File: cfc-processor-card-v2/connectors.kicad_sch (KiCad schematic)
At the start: 9 parts, among them J1 ORESAT-DEBUG-CONNECTOR-ALL, J2 J-SAMTEC-TFM-110-X1-XXX-D-RA, J4 TFM-120-01-L-D-RA, U1 RCLAMP0504FB

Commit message: Clean up CFC Processor Card from Scott's initial import which was Gerber identical to origianl EAGLE schematic. Interestingly, this version was already changed for the v2 backplane which is great. Align schematic to be more KiCAD like based off of the C3, rename a few things, remove some outdated OPD connections, import sch into pcb, clean up pcb detritus, and import DRU settings. No longer Gerber identicial, but it's now ready for further polishing for fabrication.
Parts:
- removed TP183, TP184: TEST-POINT3X4, cfc-card:PAD.03X.04, symbol cfc-card-eagle-import:TEST-POINT3X4
- removed U$1: FLIGHMARKERNEW, cfc-card:FLIGHTMARKER_NEW_BOARDS, symbol cfc-card-eagle-import:FLIGHMARKERNEW
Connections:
- net GND: no longer J4.37, J4.38
- net CAN1_H: no longer names the net of J4.33, J4.34
- net CAN1_L: no longer names the net of J4.35, J4.36
- net ~{SD}: no longer names the net of J4.39, J4.40
- new net C3-UART-RX: J4.38
- new net C3-UART-TX: J4.37
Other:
- note removed: "1.2"
- note removed: "HMM Octavo doesn't do SWD So, I might just leave these unconnected?"
- note removed: "OreSat Star Tracker: Connectors"
- company: (none) -> Portland State Aerospace Society
- title: (none) -> OreSat CFC Processor Card
- moved on the sheet: C4, J1, J4, U1

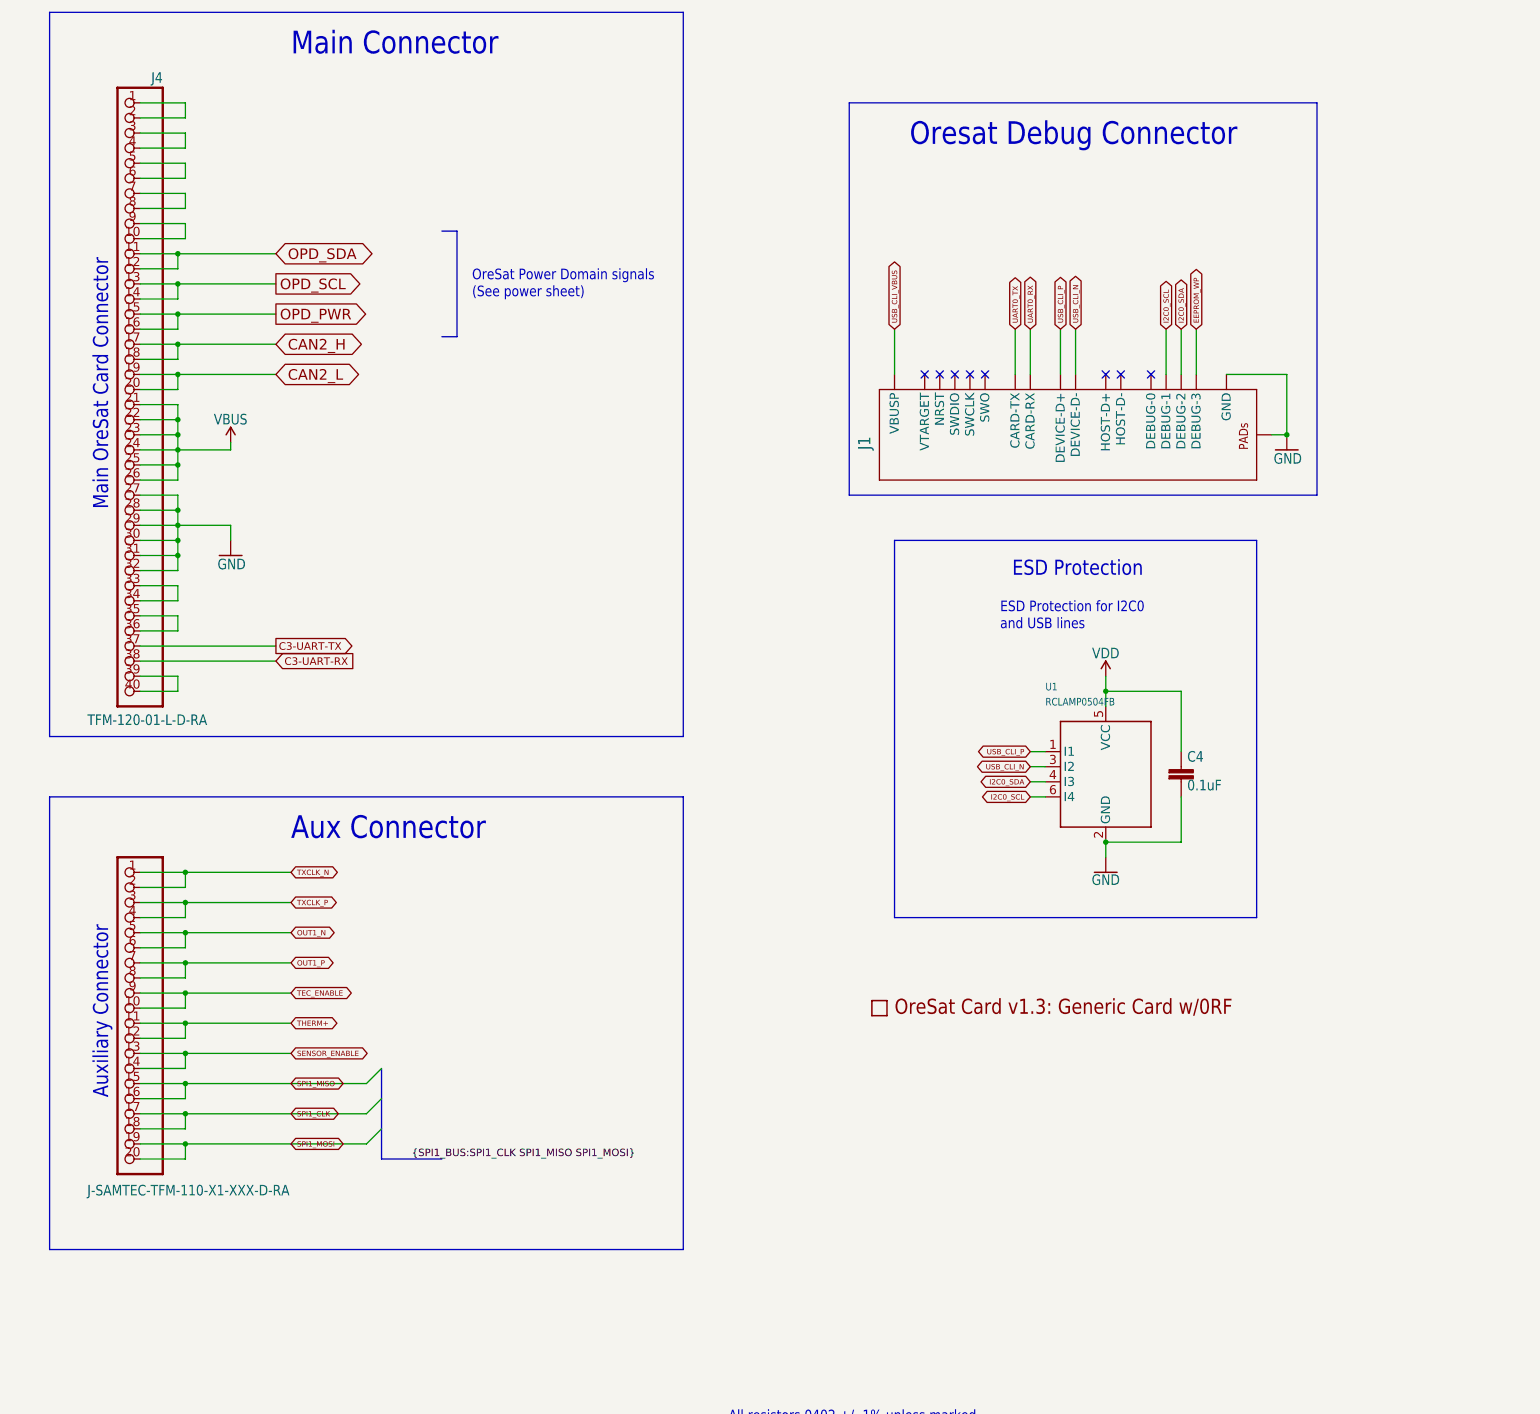
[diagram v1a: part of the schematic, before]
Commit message: Big cleanup - fixed a billion ERCs and DRCs. Switched a bunch of parts over to OreSat parts. Added analog switch on UART so CFC processor can talk serial to C3. Last thing left: clean up passives with new footprints, maybe.
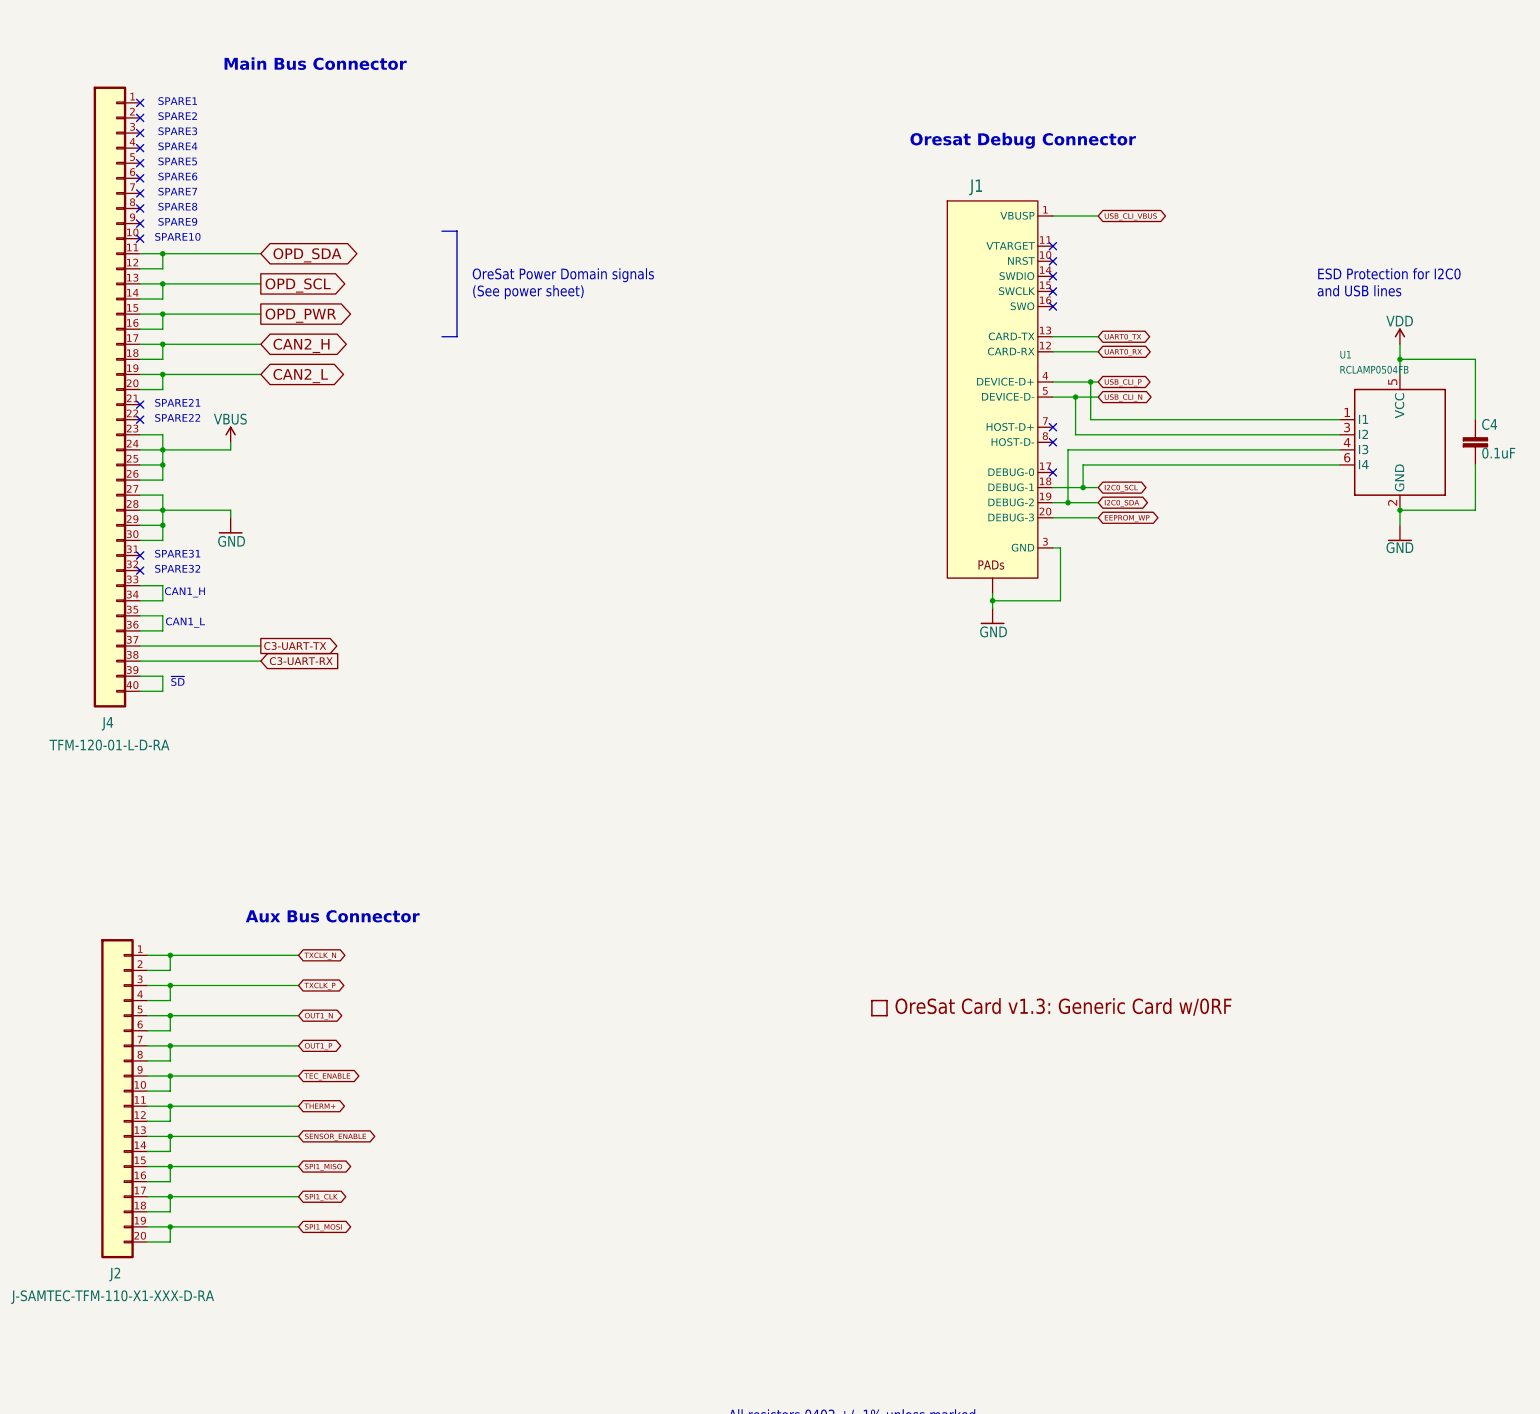
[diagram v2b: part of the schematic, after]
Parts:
- J1: footprint cfc-card:TE_2-1734592-0 -> oresat-connectors:J-TE-2-1734592-0; symbol cfc-card-eagle-import:ORESAT-DEBUG-CONNECTOR-ALL -> oresat-connectors:ORESAT-DEBUG-CONNECTOR-ALL
- J2: footprint cfc-card:J-SAMTEC-TFM-110-X1-XXX-D-RA -> oresat-connectors:J-SAMTEC-TFM-110-X1-XXX-D-RA; symbol cfc-card-eagle-import:J-SAMTEC-TFM-110-X1-XXX-D-RA -> oresat-connectors:J-SAMTEC-TFM-110-01-L-D-RA
- J4: footprint cfc-card:J-SAMTEC-TFM-120-X1-XXX-D-RA -> oresat-connectors:J-SAMTEC-TFM-120-X1-XXX-D-RA; symbol cfc-card-eagle-import:J-SAMTEC-TFM-120-X1-XXX-D-RA -> oresat-connectors:J-SAMTEC-TFM-120-01-L-D-RA
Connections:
- net GND: no longer J4.31, J4.32
- net VBUS: no longer J4.21, J4.22
- net at J4.1: no longer J4.2
- net at J4.10: no longer J4.9
- net at J4.3: no longer J4.4
- net at J4.5: no longer J4.6
- net at J4.7: no longer J4.8
- no-connect marks 8 -> 22
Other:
- note added: "Aux Bus Connector"
- note added: "CAN1_H"
- note added: "CAN1_L"
- note added: "Main Bus Connector"
- note added: "SPARE1"
- note added: "SPARE10"
- note added: "SPARE2"
- note added: "SPARE21"
- note added: "SPARE22"
- note added: "SPARE3"
- note added: "SPARE31"
- note added: "SPARE32"
- note added: "SPARE4"
- note added: "SPARE5"
- note added: "SPARE6"
- note added: "SPARE7"
- note added: "SPARE8"
- note added: "SPARE9"
- note added: "~{SD}"
- note removed: "Aux Connector"
- note removed: "Auxiliary Connector"
- note removed: "ESD Protection"
- note removed: "Main Connector"
- note removed: "Main OreSat Card Connector"
- moved on the sheet: C4, U1

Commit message: more trace polishing.
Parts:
- C4: footprint cfc-card:.0603-A -> oresat-passives:0603-C-NOSILK
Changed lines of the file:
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@@
 			)
 		)
-		(property "Footprint" "cfc-card:.0603-A"
+		(property "Footprint" "oresat-passives:0603-C-NOSILK"
 			(at 369.57 93.98 0)
 			(effects

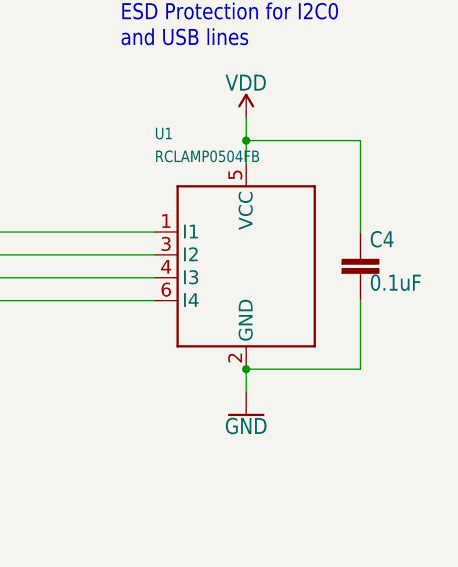
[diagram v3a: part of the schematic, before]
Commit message: More layout polishing Removed unused SPI EEPROM.
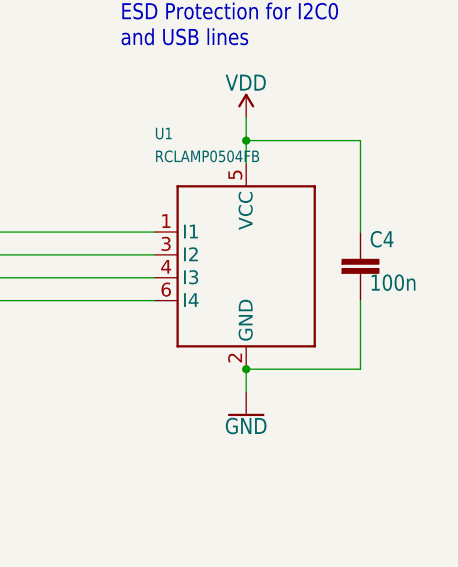
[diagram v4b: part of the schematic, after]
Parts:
- C4: value 0.1uF -> 100n
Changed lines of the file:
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@@
 			)
 		)
-		(property "Value" "0.1uF"
+		(property "Value" "100n"
 			(at 370.586 98.171 0)
 			(effects

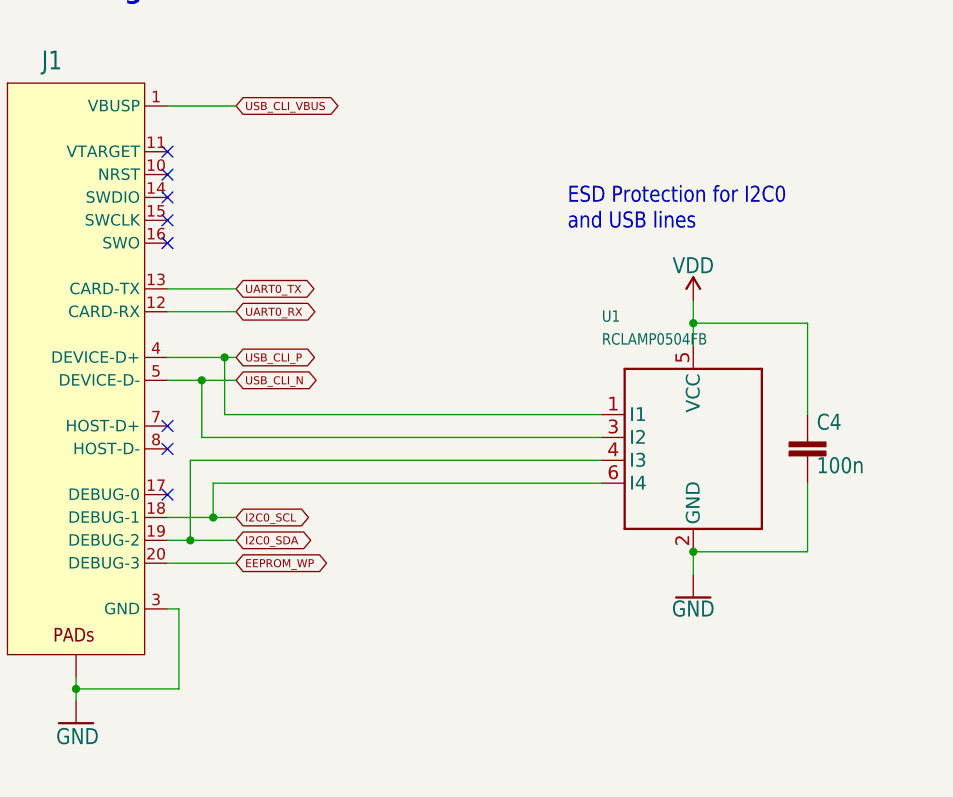
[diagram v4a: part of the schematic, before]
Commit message: Final polish on schematic and PCB. Cleaned up BOM, fixed github issues which were not really issues. Lots of BOM cleanup, with MPNs and DPNs.
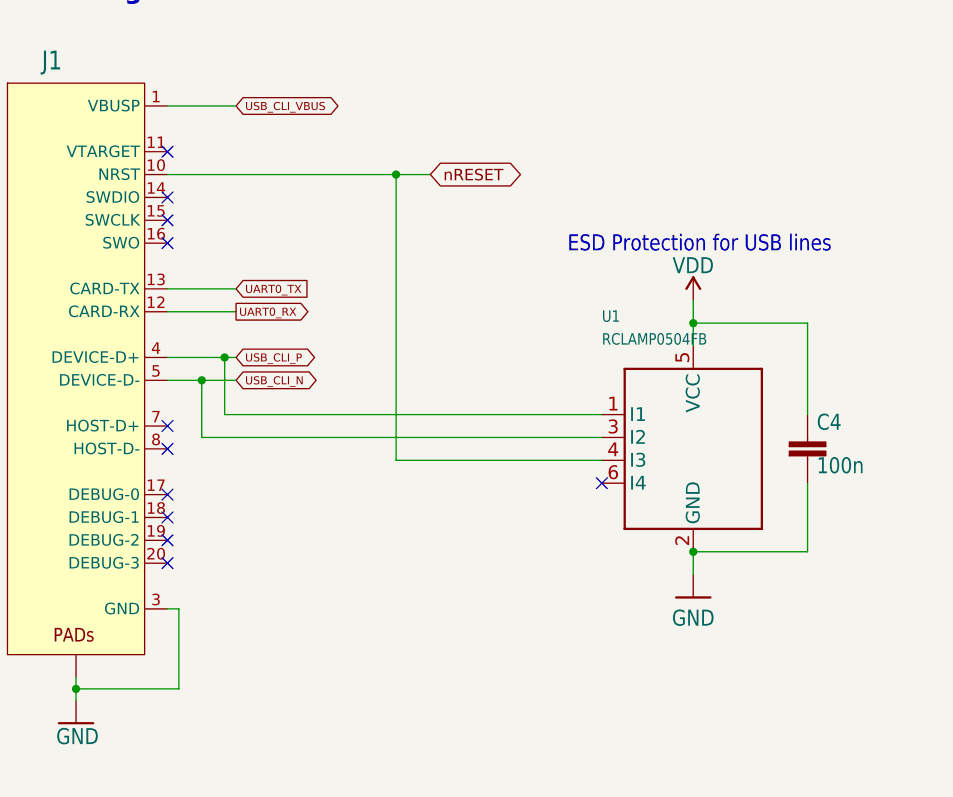
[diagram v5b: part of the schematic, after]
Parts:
- C4: DIS (none) -> DigiKey; DPN (none) -> 587-3472-1-ND; MFR (none) -> Taiyo Yuden; MPN (none) -> TMK107BJ104KAHT
- J1: value ORESAT-DEBUG-CONNECTOR-ALL -> 2-1734592-0; DIS (none) -> DigiKey; DPN (none) -> A100287CT-ND; MFR (none) -> TE Connectivity AMP Connectors; MPN (none) -> 2-1734592-0
- J4: DIS (none) -> DigiKey; DPN (none) -> SAM10145-ND; MFR (none) -> Samtec; MPN (none) -> TFM-120-01-L-D-RA
- PCB1: DIS (none) -> N/A; DPN (none) -> N/A; MFR (none) -> N/A; MPN (none) -> N/A
- U1: DIS (none) -> DigiKey; DPN (none) -> RCLAMP0504FBTCTCT-ND; MFR (none) -> Semtech Corporation; MPN (none) -> RCLAMP0504FBTCT
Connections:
- net nRESET: now reaches J1.10 (NRST)
- net nRESET: now also U1.4 (I3)
- net EEPROM_WP: no longer names the net of J1.20 (DEBUG-3)
- net I2C0_SCL: no longer names the net of U1.6 (I4)
- net I2C0_SCL: no longer J1.18 (DEBUG-1)
- net I2C0_SDA: no longer names the net of J1.19 (DEBUG-2)
- net I2C0_SDA: no longer U1.4 (I3)
- no-connect marks 22 -> 25
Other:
- note added: "ESD Protection for USB lines"
- note removed: "ESD Protection for I2C0 and USB lines"
